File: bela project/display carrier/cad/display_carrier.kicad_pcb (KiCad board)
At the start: 2 copper layers, 183.8 x 72.8 mm, 5 parts, among them U1 PocketBeagle2

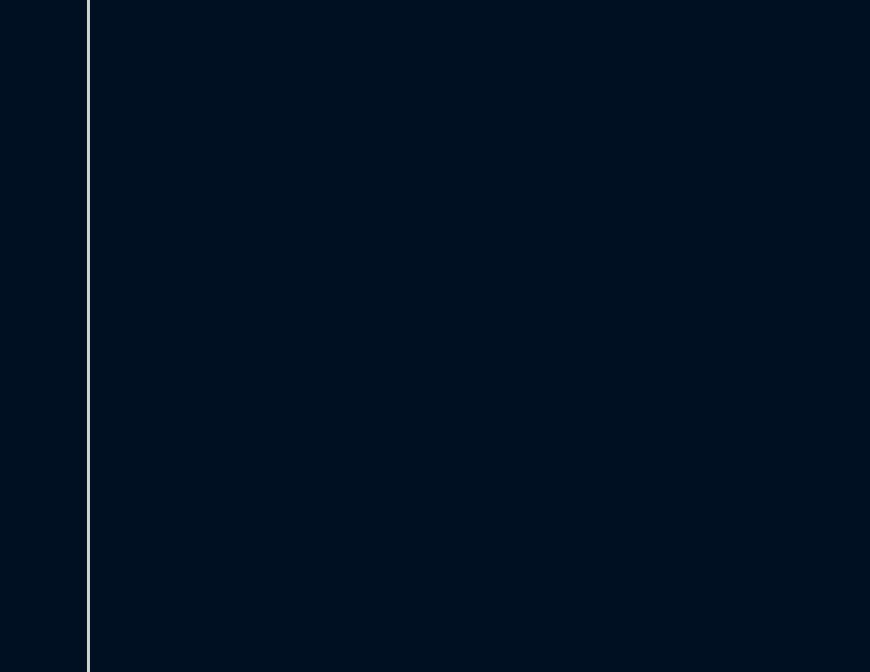
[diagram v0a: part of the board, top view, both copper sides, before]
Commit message: Display carrier: dedicated 5V power-in; PB2 sandwich now carries only GND + data
Added J_PWR (2-pin screw terminal) fed straight from the main PSU to power the two
AMOLED panels (via JA/JB). Removed +5V from the PB2 header so the display current
(~0.4-1A) no longer flows through the Beagle->Gem->carrier stack -- keeps the shared
5V/audio rail clean. PB2 now carries only common GND + the PRU data lines.

Co-Authored-By: Claude Opus 4.8 (1M context) <noreply@anthropic.com>
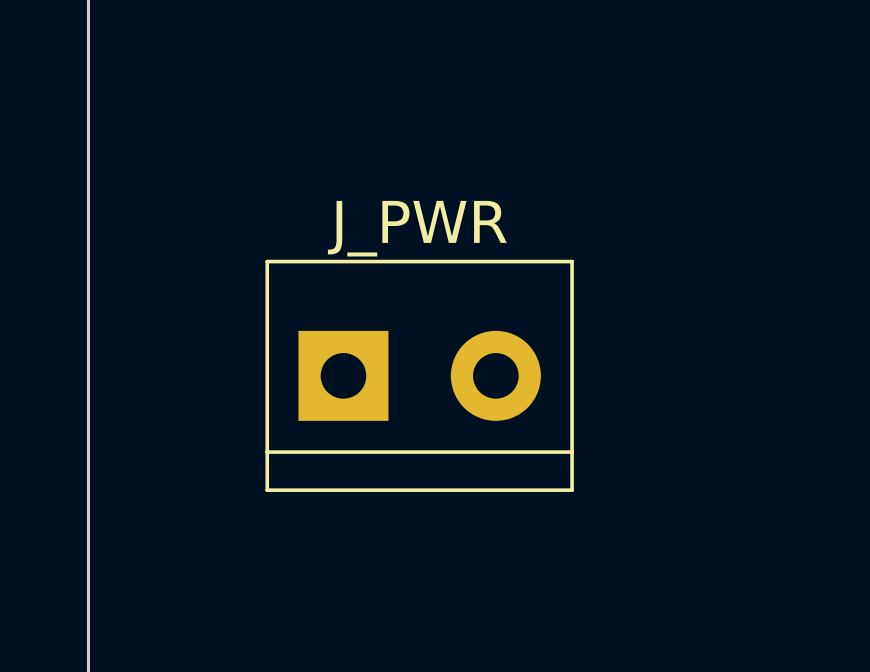
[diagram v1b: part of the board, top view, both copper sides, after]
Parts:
- added J_PWR: PWR_IN, TerminalBlock_bornier-2_P5.08mm, F.Cu at (16.0, 64.0)
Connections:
- U1 pad P2.13: +5V -> (no net)

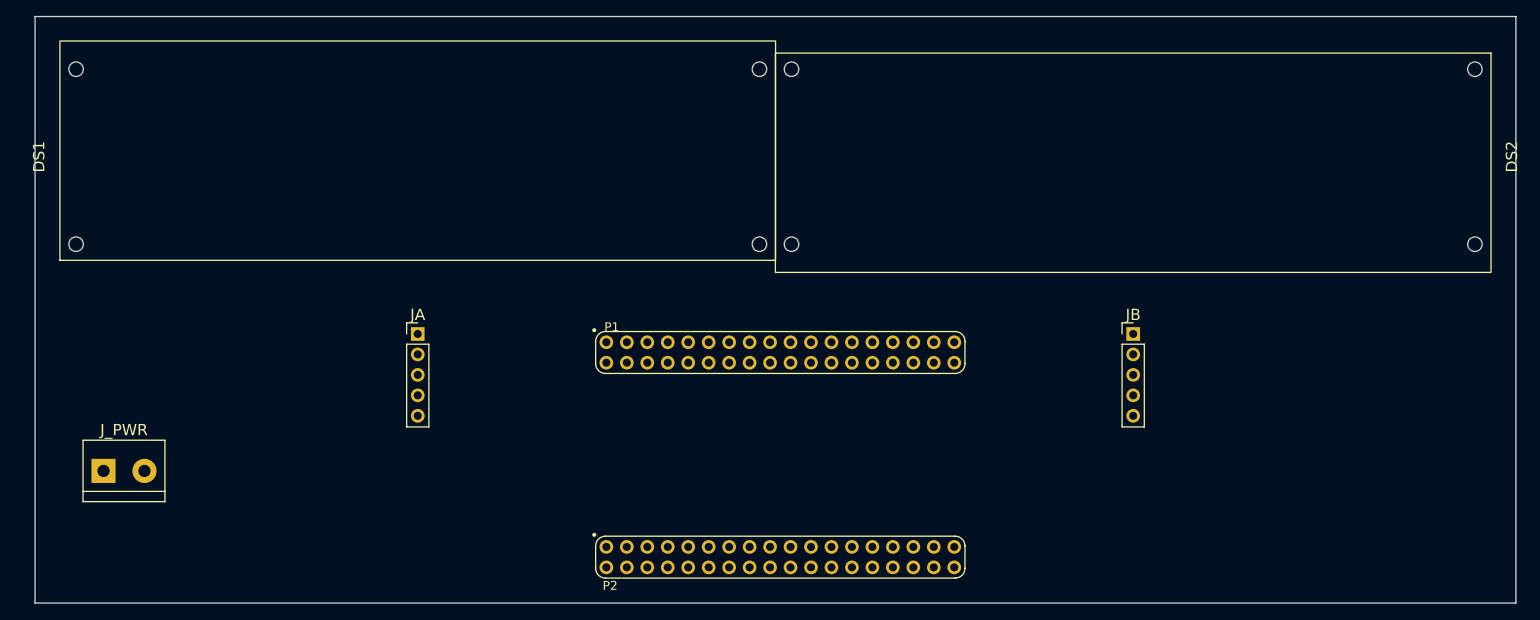
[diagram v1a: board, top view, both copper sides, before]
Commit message: display carrier: move all connectors to the back (B.Cu) so it sandwiches onto Beagle+Bela
The screen board is the TOP of the stack, so U1 (PB2 header), JA, JB and J_PWR now
sit on B.Cu and face DOWN into the sandwich; the two AMOLED displays stay on F.Cu
(up). gen_carrier.py flips the F.Cu connectors to B.Cu on a reloaded board (the big
PB2 footprint won't flip on a just-Add'ed in-memory board — SWIG quirk; PB2.kicad_mod
is natively B.Cu so it's left as-is). Adds the routed GLB export + full 4-board
ensemble renders (top / stack-side / stack-front).

Co-Authored-By: Claude Opus 4.8 (1M context) <noreply@anthropic.com>
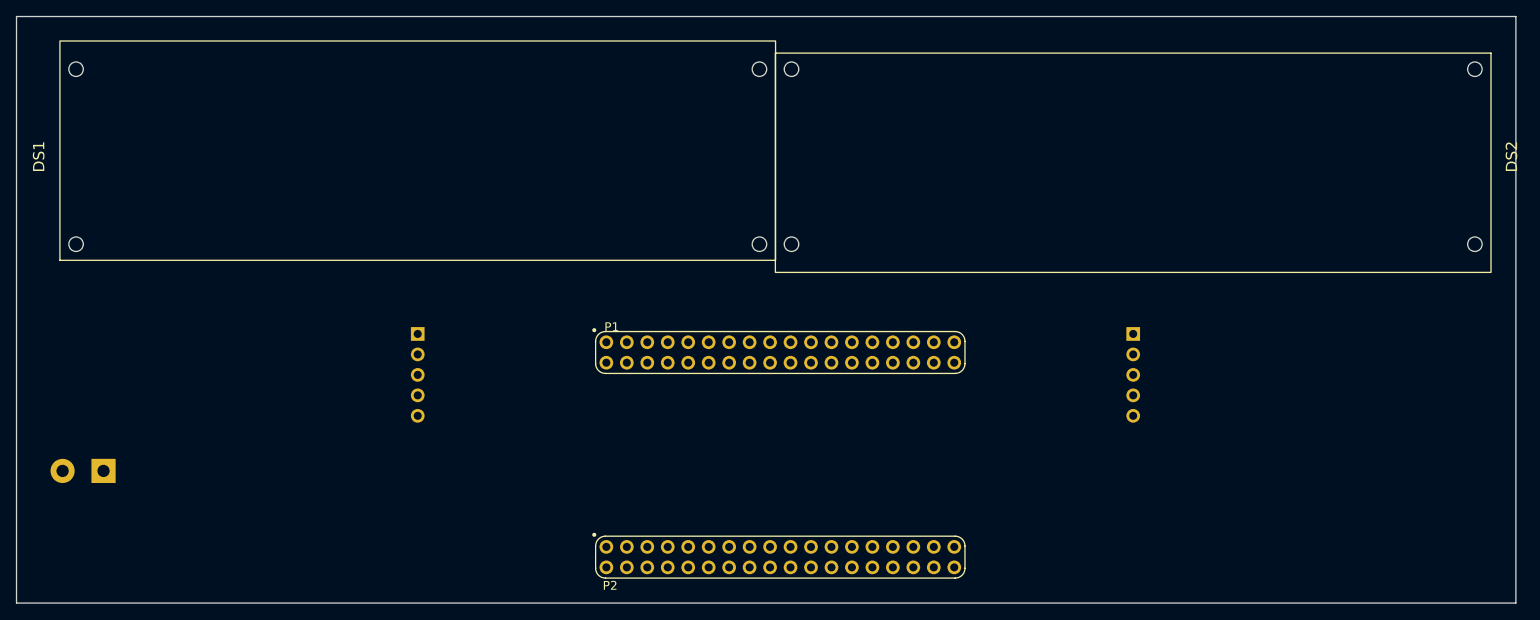
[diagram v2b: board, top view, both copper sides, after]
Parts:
- JA, JB, J_PWR: moved to B.Cu
- turned JA to 180 degrees
- turned JB to 180 degrees
- turned J_PWR to 180 degrees
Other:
- board size 183.8 x 72.8 mm -> 186.1 x 72.8 mm

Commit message: display carrier: route it (Freerouting, 0.25mm clearance sweep winner, GND both layers)
Parallel Freerouting clearance sweep {0.15,0.175,0.20,0.25mm}; 0.25mm wins as the
loosest that routes clean (most fab margin). GND poured on F.Cu+B.Cu (solid pads),
netclass 0.15 (AISLER). Result: 0 unconnected, 68 tracks, 1 via, 0 hard DRC (2
cosmetic silk only). Verified with authoritative kicad-cli DRC: 0 shorting, 0
clearance, GND filled both layers, connectors on B.Cu. Adds routing scripts
(carrier_export_dsn.py text-strips fp graphics so the DSN export doesn't choke on
the big display outlines; carrier_route_variant.py runs one clearance variant) and
the routed back-side render.

Co-Authored-By: Claude Opus 4.8 (1M context) <noreply@anthropic.com>
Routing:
- net GND: track 0.00 -> 166.8 mm
- net +5V: track 0.00 -> 143.7 mm
- net DA_TX: track 0.00 -> 65.7 mm, vias 0 -> 1
- net DA_RX: track 0.00 -> 65.0 mm
- net DB_TX: track 0.00 -> 43.5 mm
- net DB_RX: track 0.00 -> 39.9 mm
- net DA_RST: track 0.00 -> 32.4 mm
- net DB_RST: track 0.00 -> 31.7 mm
- added copper zone on B.Cu, net GND
- added copper zone on F.Cu, net GND
